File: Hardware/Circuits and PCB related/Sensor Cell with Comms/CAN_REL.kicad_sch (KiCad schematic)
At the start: 28 parts, among them J1 Conn_01x02_Shielded, U1 TCAN337, U2 MCP2518FD-xQBB, Y1 DSC6111B

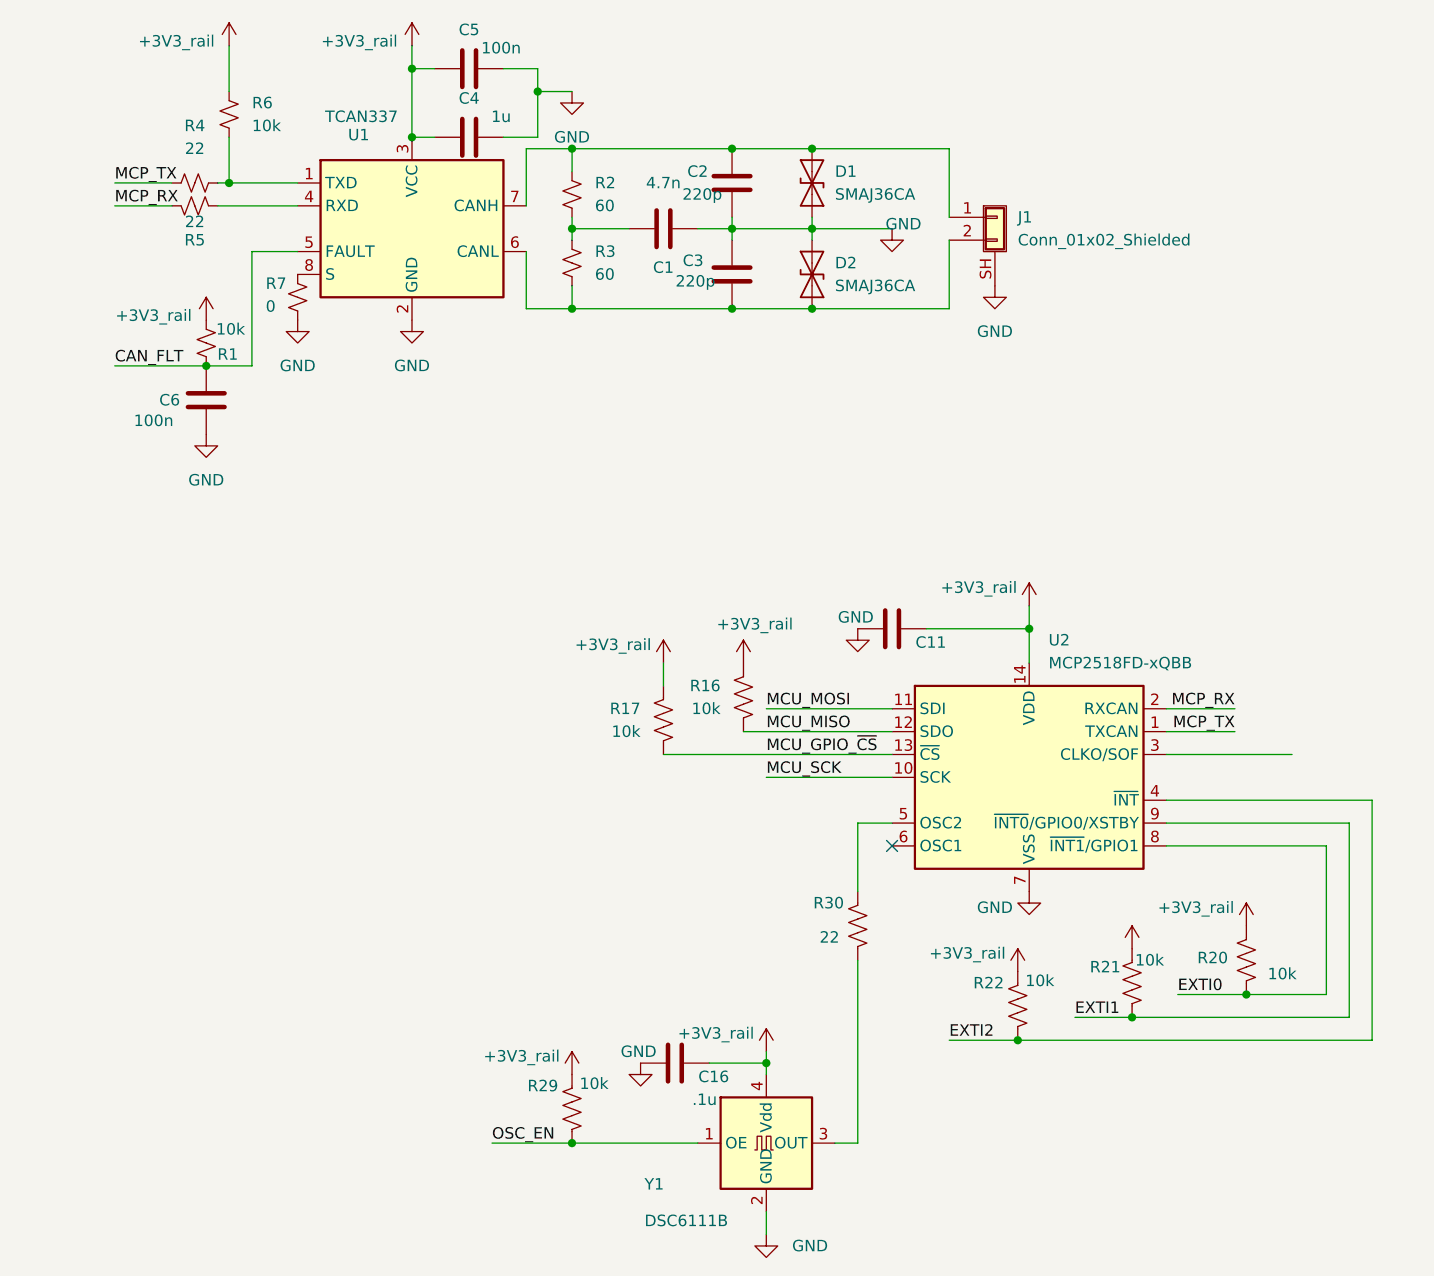
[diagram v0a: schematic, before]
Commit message: Finished schematic, added all footprints, finishing ERC now to move onto the PCB planner to have Kicad do most of the heavy lifting
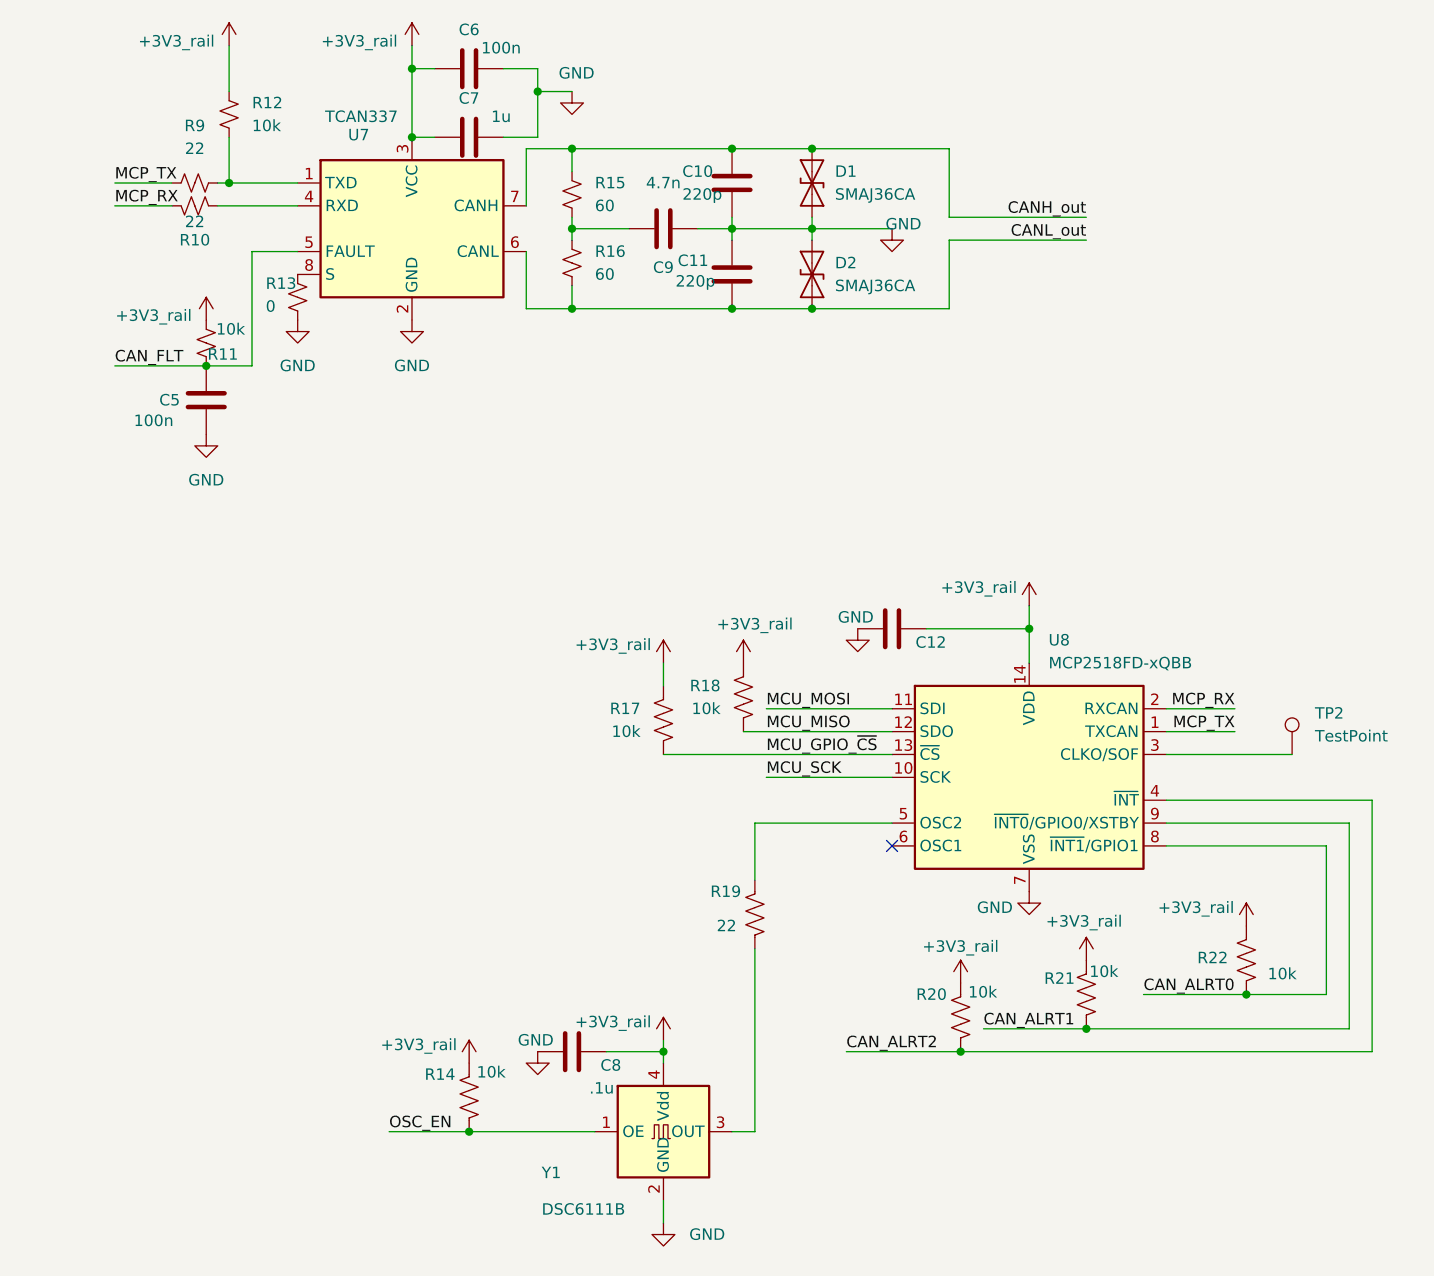
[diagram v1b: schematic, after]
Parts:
- removed J1: Conn_01x02_Shielded, symbol Connector_Generic_Shielded:Conn_01x02_Shielded
- added TP2: TestPoint, Connector_PinHeader_1.00mm:PinHeader_1x01_P1.00mm_Vertical, symbol Connector:TestPoint
- renumbered C2 to C10, C3 to C11, C11 to C12, C6 to C5, C5 to C6, C4 to C7, C16 to C8, C1 to C9, R5 to R10, R1 to R11, R6 to R12, R7 to R13, R29 to R14, R2 to R15, R3 to R16, R16 to R18, R30 to R19, R22 to R20, R20 to R22, R4 to R9, U1 to U7, U2 to U8
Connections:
- net CANH_out: now reaches C10.2, D1.2 (A2), R15.1, U7.7 (CANH)
- net at U8.3 (CLKO/SOF): now also TP2.1
- net CANL_out: now reaches C11.1, D2.1 (A1), R16.2, U7.6 (CANL)
- net EXTI0 renamed CAN_ALRT0
- net EXTI1 renamed CAN_ALRT1
- net EXTI2 renamed CAN_ALRT2
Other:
- moved on the sheet: C8, R14, R19, R20, R21, Y1

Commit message: Bulk done to resolve ERC errors, went from 70 to 25. Need to resolve the remaining errors before generation of the PCB. Decided on Hirose Electric Connectors since theyre low profile and locking
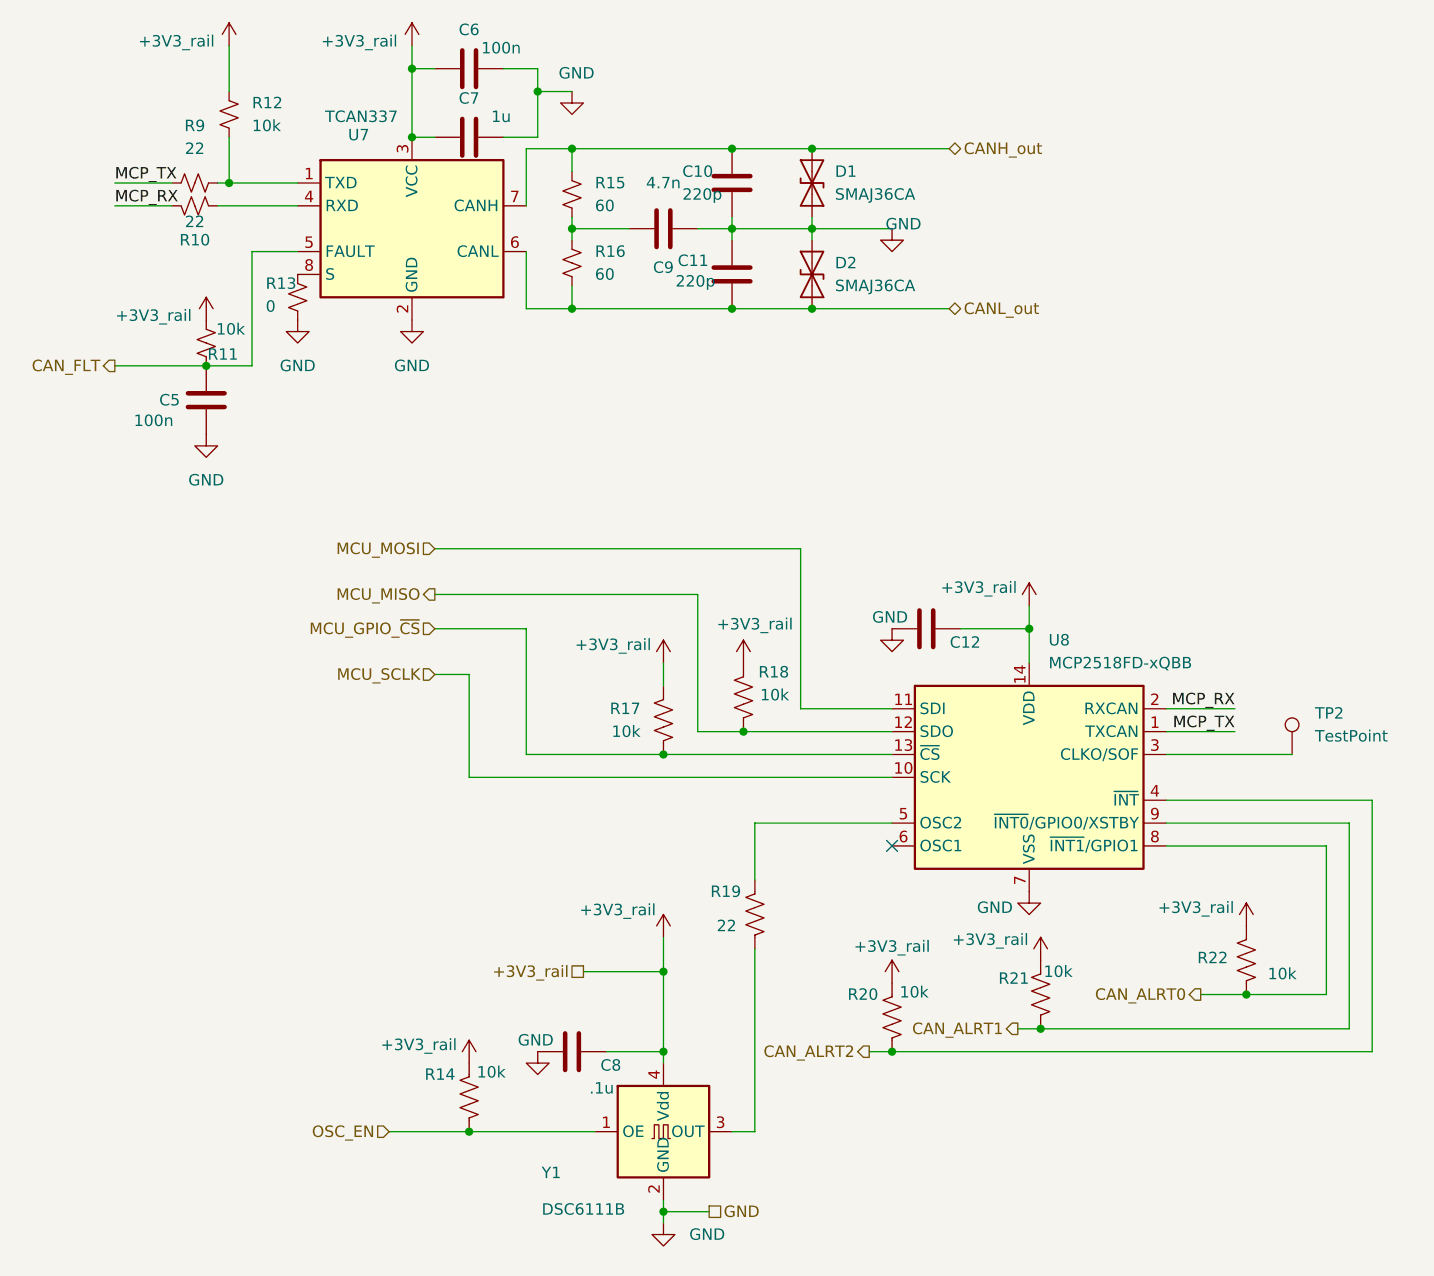
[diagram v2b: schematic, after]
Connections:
- net MCU_SCK renamed MCU_SCLK
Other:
- moved on the sheet: C12, R20, R21

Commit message: First revision of PCB nearly done, Need to finish up 1v8 planes then wire components together
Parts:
- removed D1, D2: SMAJ36CA, Diode_SMD:D_SMA, symbol Diode:SMAJ36CA
- added D1, D2: SMAJ12CA, Diode_SMD:D_SMA, symbol Diode:SMAJ12CA
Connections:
- net CANH_out: now also D1.2 (A2)
- net CANL_out: now also D2.1 (A1)
- net GND: now also D1.1 (A1), D2.2 (A2)
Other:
- title: (none) -> CAN Controller and Transciever
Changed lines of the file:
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@@
 	(generator_version "9.0")
 	(paper "A4")
+	(title_block
+		(title "CAN Controller and Transciever")
+		(date "2026-03-20")
+		(rev "1")
+	)
 	(junction
-		(at 101.6 33.02)
+		(at 110.49 50.8)
 		(diameter 0)
 		(color 0 0 0 0)
 	)
 	(junction
-		(at 83.82 41.91)
+		(at 101.6 33.02)
 		(diameter 0)
 		(color 0 0 0 0)
 	)
 	(junction
-		(at 83.82 50.8)
+		(at 83.82 41.91)
 		(diameter 0)
 		(color 0 0 0 0)
 	)
 	(junction
-		(at 134.62 86.36)
+		(at 83.82 50.8)
 		(diameter 0)
 		(color 0 0 0 0)
 	)
 	(junction
-		(at 110.49 50.8)
+		(at 134.62 86.36)
 		(diameter 0)
 		(color 0 0 0 0)
@@
 	(wire
 		(pts
-			(xy 110.49 33.02) (xy 125.73 33.02)
+			(xy 101.6 33.02) (xy 110.49 33.02)
 		)
 		(stroke
@@
 	(wire
 		(pts
-			(xy 110.49 50.8) (xy 125.73 50.8)
-		)
-		(stroke
-			(width 0)
-			(type default)
-		)
-	)
-	(wire
-		(pts
 			(xy 83.82 43.18) (xy 83.82 41.91)
 		)
@@
 	(wire
 		(pts
+			(xy 110.49 33.02) (xy 125.73 33.02)
+		)
+		(stroke
+			(width 0)
+			(type default)
+		)
+	)
+	(wire
+		(pts
 			(xy 119.38 107.95) (xy 104.14 107.95)
 		)
@@
 	(wire
 		(pts
-			(xy 101.6 33.02) (xy 110.49 33.02)
+			(xy 110.49 41.91) (xy 110.49 43.18)
 		)
 		(stroke
@@
 	(wire
 		(pts
-			(xy 110.49 41.91) (xy 110.49 43.18)
+			(xy 87.63 133.35) (xy 93.98 133.35)
 		)
 		(stroke
@@
 	(wire
 		(pts
-			(xy 87.63 133.35) (xy 93.98 133.35)
+			(xy 157.48 97.79) (xy 149.86 97.79)
 		)
 		(stroke
@@
 	(wire
 		(pts
-			(xy 157.48 97.79) (xy 149.86 97.79)
+			(xy 45.72 36.83) (xy 53.34 36.83)
 		)
 		(stroke
@@
 	(wire
 		(pts
-			(xy 45.72 36.83) (xy 53.34 36.83)
+			(xy 101.6 41.91) (xy 101.6 43.18)
 		)
 		(stroke
@@
 	(wire
 		(pts
-			(xy 101.6 41.91) (xy 101.6 43.18)
+			(xy 110.49 50.8) (xy 125.73 50.8)
 		)
 		(stroke
@@
 		(on_board yes)
 		(dnp no)
-		(fields_autoplaced yes)
 		(property "Reference" "R15"
 			(at 86.36 36.8299 0)
@@
 					(size 1.27 1.27)
 				)
-				(hide yes)
 			)
 		)
@@
 	)
 	(symbol
-		(lib_id "Diode:SMAJ36CA")
-		(at 110.49 36.83 90)
+		(lib_id "Device:R_US")
+		(at 104.14 118.11 0)
+		(mirror x)
 		(unit 1)
 		(exclude_from_sim no)
@@
 		(on_board yes)
 		(dnp no)
-		(fields_autoplaced yes)
-		(property "Reference" "D1"
-			(at 113.03 35.5599 90)
+		(property "Reference" "R19"
+			(at 102.616 115.57 0)
 			(effects
 				(font
@@
 			)
 		)
-		(property "Value" "SMAJ36CA"
-			(at 113.03 38.0999 90)
+		(property "Value" "22"
+			(at 102.108 119.38 0)
 			(effects
 				(font
@@
 			)
 		)
-		(property "Footprint" "Diode_SMD:D_SMA"
-			(at 115.57 36.83 0)
+		(property "Footprint" "Resistor_SMD:R_0603_1608Metric_Pad0.98x0.95mm_HandSolder"
+			(at 105.156 117.856 90)
 			(effects
 				(font
@@
 			)
 		)
-		(property "Datasheet" "https://www.littelfuse.com/media?resourcetype=datasheets&itemid=75e32973-b177-4ee3-a0ff-cedaf1abdb93&filename=smaj-datasheet"
-			(at 110.49 36.83 0)
+		(property "Datasheet" "~"
+			(at 104.14 118.11 0)
 			(effects
 				(font
@@
 			)
 		)
-		(property "Description" "400W bidirectional Transient Voltage Suppressor, 36.0Vr, SMA(DO-214AC)"
-			(at 110.49 36.83 0)
+		(property "Description" "Resistor, US symbol"
+			(at 104.14 118.11 0)
 			(effects
 				(font
@@
 			(project "Sensor Cell with Comms"
 				(path "/953799b5-f11e-4770-941d-f5d23acc5c6d/779df1c1-ac91-4afc-a9dd-e99c8e3614d8"
-					(reference "D1")
+					(reference "R19")
 					(unit 1)
 				)
@@
 	)
 	(symbol
-		(lib_id "Device:R_US")
-		(at 104.14 118.11 0)
-		(mirror x)
+		(lib_id "Diode:SMAJ12CA")
+		(at 110.49 36.83 90)
 		(unit 1)
 		(exclude_from_sim no)
@@
 		(on_board yes)
 		(dnp no)
-		(property "Reference" "R19"
-			(at 102.616 115.57 0)
+		(fields_autoplaced yes)
+		(property "Reference" "D1"
+			(at 113.03 35.5599 90)
 			(effects
 				(font
@@
 			)
 		)
-		(property "Value" "22"
-			(at 102.108 119.38 0)
+		(property "Value" "SMAJ12CA"
+			(at 113.03 38.0999 90)
 			(effects
 				(font
@@
 			)
 		)
-		(property "Footprint" "Resistor_SMD:R_0603_1608Metric_Pad0.98x0.95mm_HandSolder"
-			(at 105.156 117.856 90)
+		(property "Footprint" "Diode_SMD:D_SMA"
+			(at 115.57 36.83 0)
 			(effects
 				(font
@@
 			)
 		)
-		(property "Datasheet" "~"
-			(at 104.14 118.11 0)
+		(property "Datasheet" "https://www.littelfuse.com/media?resourcetype=datasheets&itemid=75e32973-b177-4ee3-a0ff-cedaf1abdb93&filename=smaj-datasheet"
+			(at 110.49 36.83 0)
 			(effects
 				(font
@@
 			)
 		)
-		(property "Description" "Resistor, US symbol"
-			(at 104.14 118.11 0)
+		(property "Description" "400W bidirectional Transient Voltage Suppressor, 12.0Vr, SMA(DO-214AC)"
+			(at 110.49 36.83 0)
 			(effects
 				(font
@@
 			(project "Sensor Cell with Comms"
 				(path "/953799b5-f11e-4770-941d-f5d23acc5c6d/779df1c1-ac91-4afc-a9dd-e99c8e3614d8"
-					(reference "R19")
+					(reference "D1")
 					(unit 1)
 				)
@@
 	)
 	(symbol
+		(lib_id "Diode:SMAJ12CA")
+		(at 110.49 46.99 90)
+		(unit 1)
+		(exclude_from_sim no)
+		(in_bom yes)
+		(on_board yes)
+		(dnp no)
+		(fields_autoplaced yes)
+		(property "Reference" "D2"
+			(at 113.03 45.7199 90)
+			(effects
+				(font
+					(size 1.27 1.27)
+				)
+				(justify right)
+			)
+		)
+		(property "Value" "SMAJ12CA"
+			(at 113.03 48.2599 90)
+			(effects
+				(font
+					(size 1.27 1.27)
+				)
+				(justify right)
+			)
+		)
+		(property "Footprint" "Diode_SMD:D_SMA"
+			(at 115.57 46.99 0)
+			(effects
+				(font
+					(size 1.27 1.27)
+				)
+				(hide yes)
+			)
+		)
+		(property "Datasheet" "https://www.littelfuse.com/media?resourcetype=datasheets&itemid=75e32973-b177-4ee3-a0ff-cedaf1abdb93&filename=smaj-datasheet"
+			(at 110.49 46.99 0)
+			(effects
+				(font
+					(size 1.27 1.27)
+				)
+				(hide yes)
+			)
+		)
+		(property "Description" "400W bidirectional Transient Voltage Suppressor, 12.0Vr, SMA(DO-214AC)"
+			(at 110.49 46.99 0)
+			(effects
+				(font
+					(size 1.27 1.27)
+				)
+				(hide yes)
+			)
+		)
+		(pin "2"
+		)
+		(pin "1"
+		)
+		(instances
+			(project "Sensor Cell with Comms"
+				(path "/953799b5-f11e-4770-941d-f5d23acc5c6d/779df1c1-ac91-4afc-a9dd-e99c8e3614d8"
+					(reference "D2")
+					(unit 1)
+				)
+			)
+		)
+	)
+	(symbol
 		(lib_id "power:+3V3")
 		(at 43.18 52.07 0)
@@
 					(unit 1)
 				)
-			)
-		)
-	)
-	(symbol
-		(lib_id "Diode:SMAJ36CA")
-		(at 110.49 46.99 90)
-		(unit 1)
-		(exclude_from_sim no)
-		(in_bom yes)
-		(on_board yes)
-		(dnp no)
-		(fields_autoplaced yes)
-		(property "Reference" "D2"
-			(at 113.03 45.7199 90)
-			(effects
-				(font
-					(size 1.27 1.27)
-				)
-				(justify right)
-			)
-		)
-		(property "Value" "SMAJ36CA"
-			(at 113.03 48.2599 90)
-			(effects
-				(font
-					(size 1.27 1.27)
-				)
-				(justify right)
-			)
-		)
-		(property "Footprint" "Diode_SMD:D_SMA"
-			(at 115.57 46.99 0)
-			(effects
-				(font
-					(size 1.27 1.27)
-				)
-				(hide yes)
-			)
-		)
-		(property "Datasheet" "https://www.littelfuse.com/media?resourcetype=datasheets&itemid=75e32973-b177-4ee3-a0ff-cedaf1abdb93&filename=smaj-datasheet"
-			(at 110.49 46.99 0)
-			(effects
-				(font
-					(size 1.27 1.27)
-				)
-				(hide yes)
-			)
-		)
-		(property "Description" "400W bidirectional Transient Voltage Suppressor, 36.0Vr, SMA(DO-214AC)"
-			(at 110.49 46.99 0)
-			(effects
-				(font
-					(size 1.27 1.27)
-				)
-				(hide yes)
-			)
-		)
-		(pin "2"
-		)
-		(pin "1"
-		)
-		(instances
-			(project "Sensor Cell with Comms"
-				(path "/953799b5-f11e-4770-941d-f5d23acc5c6d/779df1c1-ac91-4afc-a9dd-e99c8e3614d8"
-					(reference "D2")
-					(unit 1)
-				)
